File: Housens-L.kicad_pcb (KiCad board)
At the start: 4 copper layers, 50 x 50 mm, 54 parts, among them J1 JTAG/SWD, J2 USB_C_2.0, J3 RPI_SWD, J4 RPI_SWD, SW1 RESET, SW2 USER, U1 LM3670MF, U2 BME280, U3 OPT3005, U4 STM32WB55CGUx, U5 STCC4, U6 REG710NA-3.3, U7 AP22966, U8 MLPF-WB55-01E3, Y1 32MHz, Y2 32.768kHz

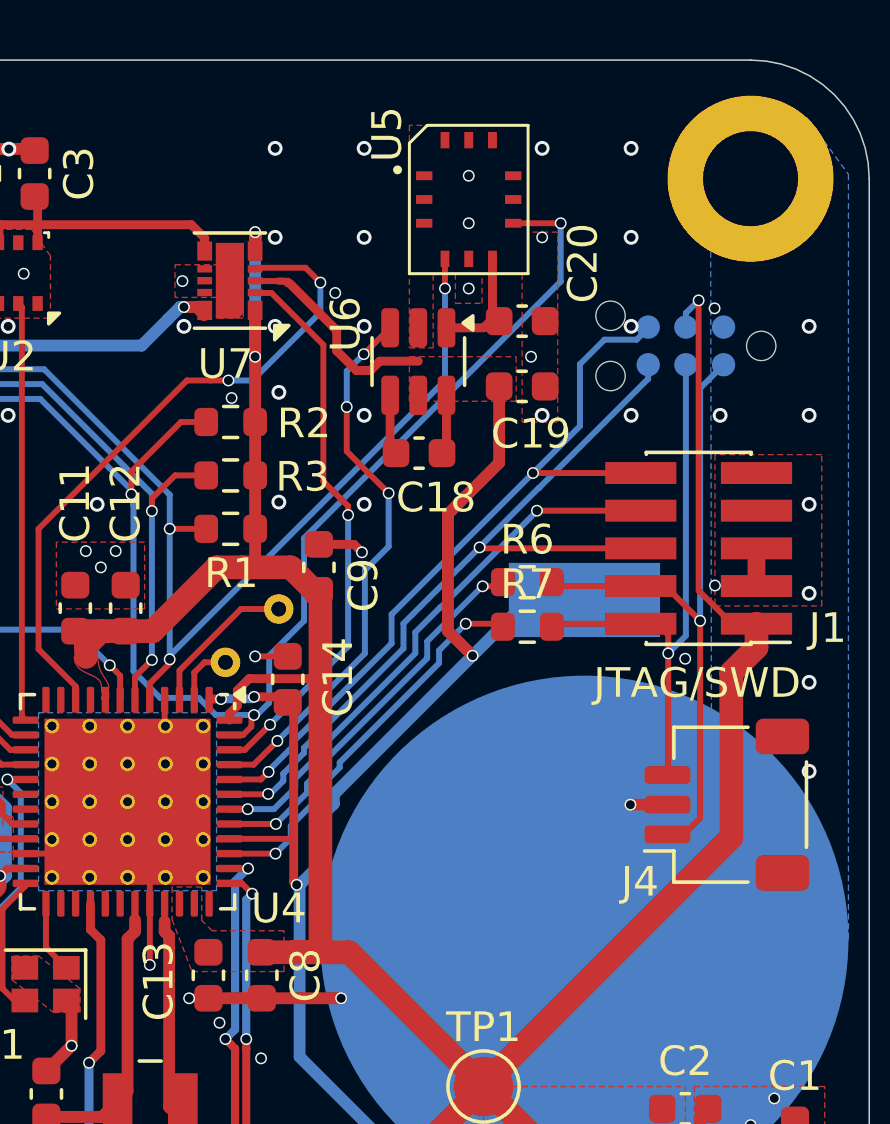
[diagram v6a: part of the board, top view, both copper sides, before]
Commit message: Make STCC4 silk prettier
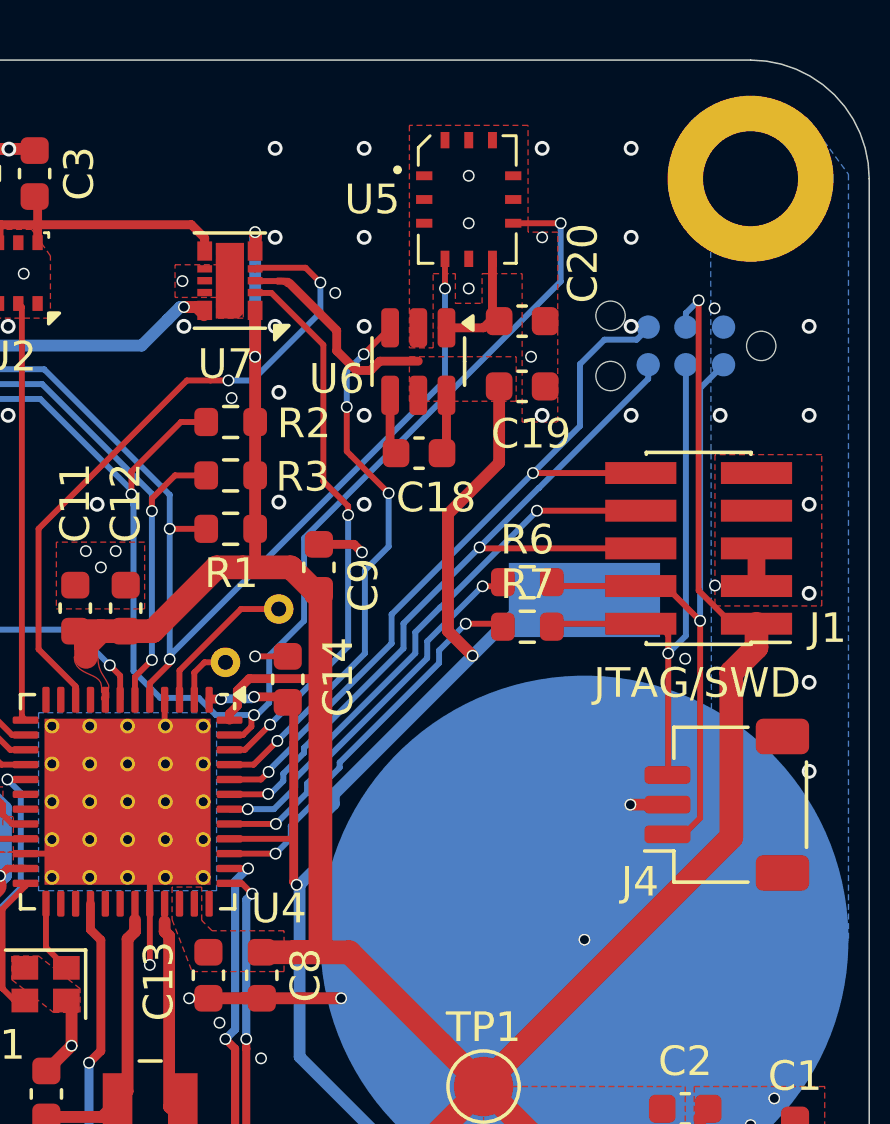
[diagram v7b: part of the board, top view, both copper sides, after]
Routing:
- net GND: vias 160 -> 161
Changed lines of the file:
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@@
 		(tags "SOT TO_SOT_SMD")
 		(property "Reference" "U6"
-			(at -1.2625 2.45 -90)
+			(at 0.5875 2.75 0)
 			(layer "F.SilkS")
 			(effects
@@
 		(at 96.5 84.7)
 		(property "Reference" "U5"
-			(at -2.75 -2.2 90)
+			(at -3.25 0 0)
 			(unlocked yes)
 			(layer "F.SilkS")
@@
 		(attr smd)
 		(fp_line
-			(start -2 -1.9)
-			(end -2 2.5)
+			(start -1.7 -1.75)
+			(end -1.7 -1.15)
 			(stroke
 				(width 0.1)
@@
 		)
 		(fp_line
-			(start -2 2.5)
-			(end 2 2.5)
+			(start -1.7 1.2)
+			(end -1.7 2.15)
 			(stroke
 				(width 0.1)
@@
 		)
 		(fp_line
-			(start -1.4 -2.5)
-			(end -2 -1.9)
+			(start -1.7 2.15)
+			(end -1.2 2.15)
 			(stroke
 				(width 0.1)
@@
 		)
 		(fp_line
-			(start 2 -2.5)
-			(end -1.4 -2.5)
+			(start -1.3 -2.15)
+			(end -1.7 -1.75)
 			(stroke
 				(width 0.1)
@@
 		)
 		(fp_line
-			(start 2 2.5)
-			(end 2 -2.5)
+			(start 1.2 2.15)
+			(end 1.6 2.15)
+			(stroke
+				(width 0.1)
+				(type default)
+			)
+			(layer "F.SilkS")
+		)
+		(fp_line
+			(start 1.6 -2.15)
+			(end 1.15 -2.15)
+			(stroke
+				(width 0.1)
+				(type default)
+			)
+			(layer "F.SilkS")
+		)
+		(fp_line
+			(start 1.6 -1.15)
+			(end 1.6 -2.1)
+			(stroke
+				(width 0.1)
+				(type default)
+			)
+			(layer "F.SilkS")
+		)
+		(fp_line
+			(start 1.6 2.15)
+			(end 1.6 1.15)
 			(stroke
 				(width 0.1)
@@
 			(layer "F.SilkS")
 		)
+		(fp_line
+			(start -2 -1.9)
+			(end -2 2.5)
+			(stroke
+				(width 0.1)
+				(type default)
+			)
+			(layer "Dwgs.User")
+		)
+		(fp_line
+			(start -2 2.5)
+			(end 2 2.5)
+			(stroke
+				(width 0.1)
+				(type default)
+			)
+			(layer "Dwgs.User")
+		)
+		(fp_line
+			(start -1.4 -2.5)
+			(end -2 -1.9)
+			(stroke
+				(width 0.1)
+				(type default)
+			)
+			(layer "Dwgs.User")
+		)
+		(fp_line
+			(start 2 -2.5)
+			(end -1.4 -2.5)
+			(stroke
+				(width 0.1)
+				(type default)
+			)
+			(layer "Dwgs.User")
+		)
+		(fp_line
+			(start 2 2.5)
+			(end 2 -2.5)
+			(stroke
+				(width 0.1)
+				(type default)
+			)
+			(layer "Dwgs.User")
+		)
 		(fp_rect
 			(start -2.5 -3)
@@
 		(tags "tag connect programming header pogo pins")
 		(property "Reference" "J3"
-			(at 0 -2.7 360)
+			(at 0 -2.7 0)
 			(layer "B.SilkS")
 			(hide yes)
@@
 		)
 		(property "Value" "RPI_SWD"
-			(at 0 2.3 360)
+			(at 0 2.3 0)
 			(layer "B.Fab")
 			(hide yes)
@@
 		)
 		(fp_text user "KEEPOUT"
-			(at 0 0 360)
+			(at 0 0 0)
 			(layer "Cmts.User")
 			(effects
@@
 		)
 		(fp_text user "${REFERENCE}"
-			(at 0 0 360)
+			(at 0 0 0)
 			(layer "B.Fab")
 			(effects
@@
 		(net 2)
 	)
+	(via
+		(at 100.4 109.65)
+		(size 0.4)
+		(drill 0.3)
+		(layers "F.Cu" "B.Cu")
+		(remove_unused_layers yes)
+		(keep_end_layers no)
+		(zone_layer_connections "In1.Cu" "In2.Cu")
+		(net 2)
+	)

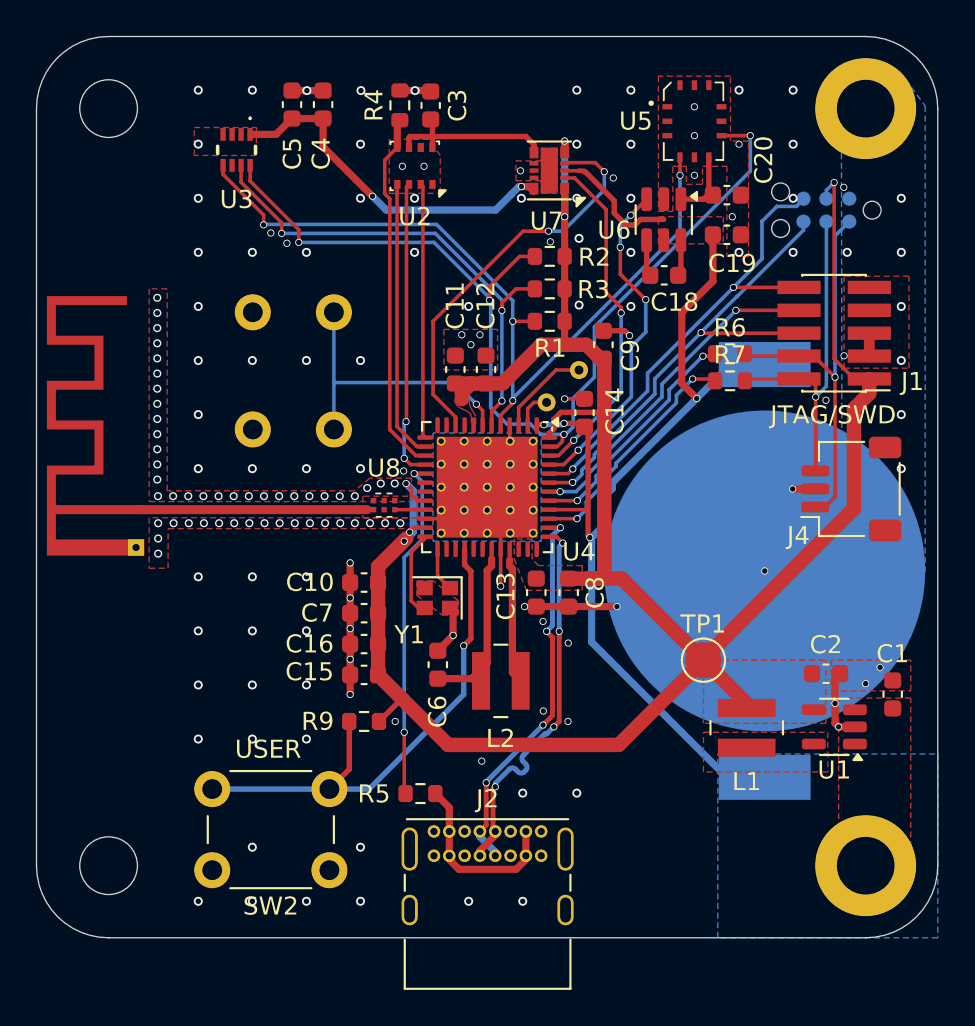
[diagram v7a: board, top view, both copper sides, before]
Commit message: Restitch at 1/20th wavelength
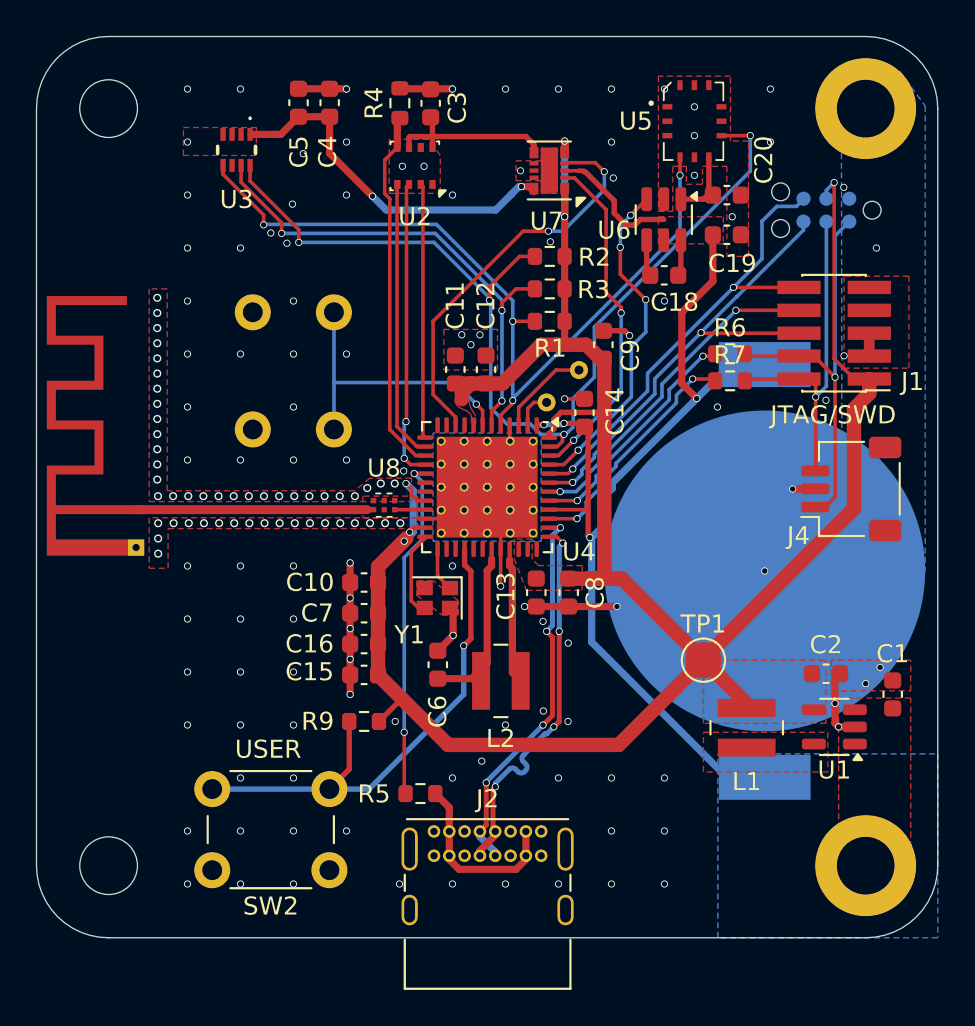
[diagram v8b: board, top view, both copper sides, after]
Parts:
- moved C4 0.38 mm to (76.3, 83.7)
- moved C5 0.38 mm to (74.5, 83.7)
- moved C3 0.12 mm to (81.9, 83.7)
- moved R4 0.12 mm to (80.2, 83.7)
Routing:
- net GND: track 39.9 -> 42.2 mm, vias 161 -> 159
